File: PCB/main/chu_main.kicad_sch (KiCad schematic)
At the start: 112 parts, among them J1 Conn_01x04, K1 Conn_01x01_Female, K10 Conn_01x01_Female, K11 Conn_01x01_Female, K12 Conn_01x01_Female, K13 Conn_01x01_Female, K14 Conn_01x01_Female, K15 Conn_01x01_Female, K16 Conn_01x01_Female, K17 Conn_01x01_Female, K18 Conn_01x01_Female, K19 Conn_01x01_Female, K2 Conn_01x01_Female, K20 Conn_01x01_Female, K21 Conn_01x01_Female, K22 Conn_01x01_Female, K23 Conn_01x01_Female, K24 Conn_01x01_Female, K25 Conn_01x01_Female, K26 Conn_01x01_Female, K27 Conn_01x01_Female, K28 Conn_01x01_Female, K29 Conn_01x01_Female, K3 Conn_01x01_Female, K30 Conn_01x01_Female, K31 Conn_01x01_Female, K32 Conn_01x01_Female, K4 Conn_01x01_Female, K5 Conn_01x01_Female, K6 Conn_01x01_Female, K7 Conn_01x01_Female, K8 Conn_01x01_Female, K9 Conn_01x01_Female, U0 ChuAcrylic, U1 Pico, U2 PCA9548APW, U3 MPR121QR2_BOARD, U4 MPR121QR2_BOARD, U5 MPR121QR2_BOARD, U8 SN74LV1T34DBV, X1 GP2Y0E03_REAL, X2 GP2Y0E03_REAL, X3 GP2Y0E03_REAL, X4 GP2Y0E03_REAL, X5 GP2Y0E03_REAL

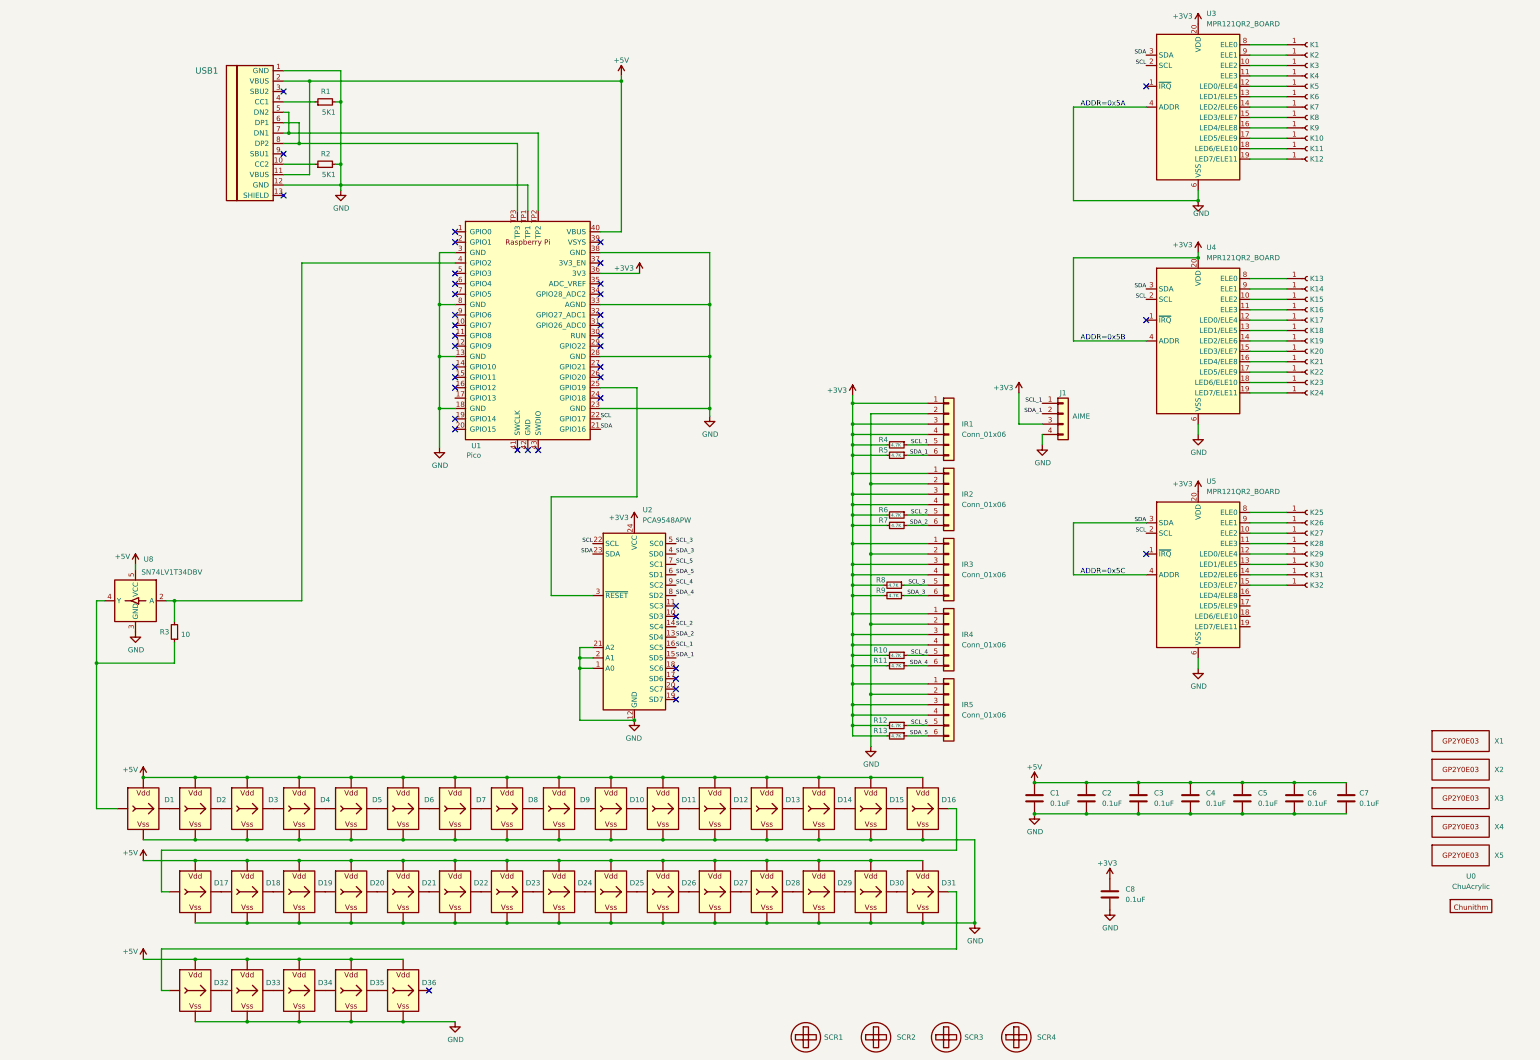
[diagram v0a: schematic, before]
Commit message: wip full size pcb with hc-sr04 ultrasonic sensors
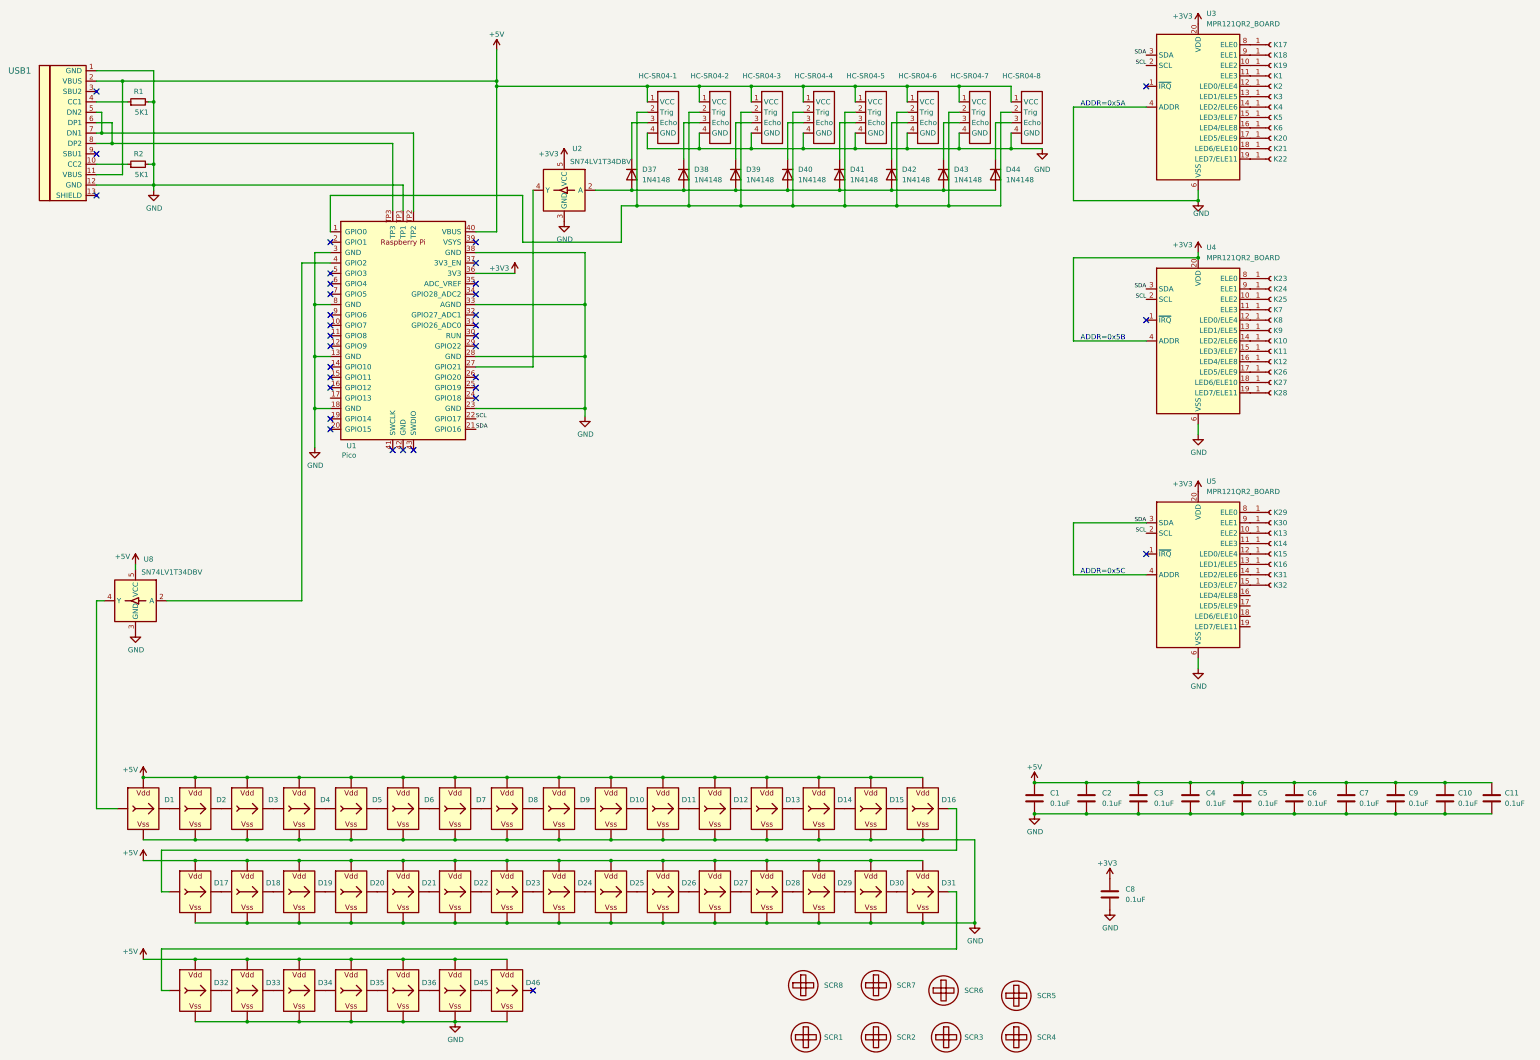
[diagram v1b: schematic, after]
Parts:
- removed IR1, IR2, IR3, IR4, IR5: Conn_01x06, chu_main:GP2Y0E03, symbol Connector_Generic:Conn_01x06
- removed J1: Conn_01x04, chu_main:PN532, symbol Connector_Generic:Conn_01x04
- removed R10, R11, R12, R13, R4, R5, R6, R7, R8, R9: 4.7K, Resistor_SMD:R_0603_1608Metric, symbol Device:R_Small
- removed R3: 10, Resistor_SMD:R_0603_1608Metric, symbol Device:R_Small
- removed U0: ChuAcrylic, chu_main:ChuAcrylic, symbol chu_main:ChuAcrylic
- removed U2: PCA9548APW, Package_SO:TSSOP-24_4.4x7.8mm_P0.65mm, symbol Interface_Expansion:PCA9548APW
- removed X1, X2, X3, X4, X5: GP2Y0E03_REAL, chu_main:GP2Y0E03_REAL, symbol chu_main:GP2Y0E03_REAL
- added C10, C11, C9: 0.1uF, Capacitor_SMD:C_0603_1608Metric_Pad1.08x0.95mm_HandSolder, symbol Device:C
- added D37, D38, D39, D40, D41, D42, D43, D44: 1N4148, Diode_THT:D_DO-35_SOD27_P7.62mm_Horizontal, symbol Diode:1N4148
- added D45, D46: WS2812B_Unified, chu_main:WS2812D-F5, symbol chu_main:WS2812B_Unified
- added HC-SR04-1, HC-SR04-2, HC-SR04-3, HC-SR04-4, HC-SR04-5, HC-SR04-6, HC-SR04-7, HC-SR04-8: ~, HC-SR04:HC-SR04, symbol chu_main:HC-SR04
- added SCR5, SCR6, SCR7, SCR8: ScrewHole, chu_main:MountingHole_3.2mm_M3, symbol iidx_teeny:ScrewHole
- added U2: SN74LV1T34DBV, chu_main:SOT-23-5_Jumper, symbol Logic_LevelTranslator:SN74LV1T34DBV
- D1, D10, D11, D12, D13, D14, D15, D16, D17, D18, D19, D2, D20, D21, D22, D23, D24, D25, D26, D27, D28, D29, D3, D30, D31, D32, D33, D34, D35, D36, D4, D5, D6, D7, D8, D9: footprint chu_main:WS2812B-4020 -> chu_main:WS2812D-F5
- K1, K10, K15, K16, K17, K18, K19, K2, K20, K21, K22, K27, K28, K29, K3, K30, K31, K32, K4, K5, K6, K7, K8, K9: footprint chu_main:ChuKey -> chu_main:Chu_TouchKey
- K11, K14, K23, K26: footprint chu_main:ChuKeyBiasLeft -> chu_main:Chu_TouchKey
- K12, K13, K24, K25: footprint chu_main:ChuKeyBiasRight -> chu_main:Chu_TouchKey
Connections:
- net +3V3: now also U2.5 (VCC)
- net +5V: now also C10.1, C11.1, C9.1, D45.V (VDD), D46.V (VDD), HC-SR04-1.1 (VCC), HC-SR04-2.1 (VCC), HC-SR04-3.1 (VCC), HC-SR04-4.1 (VCC), HC-SR04-5.1 (VCC), HC-SR04-6.1 (VCC), HC-SR04-7.1 (VCC), HC-SR04-8.1 (VCC)
- net GND: now also C10.2, C11.2, C9.2, D45.G (VSS), D46.G (VSS), HC-SR04-1.4 (GND), HC-SR04-2.4 (GND), HC-SR04-3.4 (GND), HC-SR04-4.4 (GND), HC-SR04-5.4 (GND), HC-SR04-6.4 (GND), HC-SR04-7.4 (GND), HC-SR04-8.4 (GND), U2.3 (GND)
- net at U1.1 (GPIO0): now also HC-SR04-1.2 (Trig), HC-SR04-2.2 (Trig), HC-SR04-3.2 (Trig), HC-SR04-4.2 (Trig), HC-SR04-5.2 (Trig), HC-SR04-6.2 (Trig), HC-SR04-7.2 (Trig), HC-SR04-8.2 (Trig)
- net at U1.27 (GPIO21): now also U2.4 (Y)
- net at K11.1 (Pin_1): now also U4.15 (LED3/ELE7); no longer U3.18 (LED6/ELE10)
- net at K3.1 (Pin_1): now also U3.13 (LED1/ELE5); no longer U3.10 (ELE2)
- net at K14.1 (Pin_1): now also U5.11 (ELE3); no longer U4.9 (ELE1)
- net at K29.1 (Pin_1): now also U5.8 (ELE0); no longer U5.12 (LED0/ELE4)
- net at K30.1 (Pin_1): now also U5.9 (ELE1); no longer U5.13 (LED1/ELE5)
- net at K1.1 (Pin_1): now also U3.11 (ELE3); no longer U3.8 (ELE0)
- net at K7.1 (Pin_1): now also U4.11 (ELE3); no longer U3.14 (LED2/ELE6)
- net at K27.1 (Pin_1): now also U4.18 (LED6/ELE10); no longer U5.10 (ELE2)
- net at K19.1 (Pin_1): now also U3.10 (ELE2); no longer U4.14 (LED2/ELE6)
- net at K6.1 (Pin_1): now also U3.16 (LED4/ELE8); no longer U3.13 (LED1/ELE5)
- net at K15.1 (Pin_1): now also U5.12 (LED0/ELE4); no longer U4.10 (ELE2)
- net at K5.1 (Pin_1): now also U3.15 (LED3/ELE7); no longer U3.12 (LED0/ELE4)
- net at K23.1 (Pin_1): now also U4.8 (ELE0); no longer U4.18 (LED6/ELE10)
- net at K16.1 (Pin_1): now also U5.13 (LED1/ELE5); no longer U4.11 (ELE3)
- net at U4.12 (LED0/ELE4): now also K8.1 (Pin_1); no longer K17.1 (Pin_1)
- net at U4.13 (LED1/ELE5): now also K9.1 (Pin_1); no longer K18.1 (Pin_1)
- net at K20.1 (Pin_1): now also U3.17 (LED5/ELE9); no longer U4.15 (LED3/ELE7)
- net at U4.16 (LED4/ELE8): now also K12.1 (Pin_1); no longer K21.1 (Pin_1)
- net at U4.17 (LED5/ELE9): now also K26.1 (Pin_1); no longer K22.1 (Pin_1)
- net at U4.19 (LED7/ELE11): now also K28.1 (Pin_1); no longer K24.1 (Pin_1)
- net at K13.1 (Pin_1): now also U5.10 (ELE2); no longer U4.8 (ELE0)
- net at K10.1 (Pin_1): now also U4.14 (LED2/ELE6); no longer U3.17 (LED5/ELE9)
- net at K4.1 (Pin_1): now also U3.14 (LED2/ELE6); no longer U3.11 (ELE3)
- net at U3.19 (LED7/ELE11): now also K22.1 (Pin_1); no longer K12.1 (Pin_1)
- net at K2.1 (Pin_1): now also U3.12 (LED0/ELE4); no longer U3.9 (ELE1)
- net at K25.1 (Pin_1): now also U4.10 (ELE2); no longer U5.8 (ELE0)
- net at D36.O (Out): now also D45.I (In)
- new net: D44.1 (K), HC-SR04-8.3 (Echo)
- new net: D37.1 (K), HC-SR04-1.3 (Echo)
- new net: D43.1 (K), HC-SR04-7.3 (Echo)
- new net: D37.2 (A), D38.2 (A), D39.2 (A), D40.2 (A), D41.2 (A), D42.2 (A), D43.2 (A), D44.2 (A), U2.2 (A)
- new net: D45.O (Out), D46.I (In)
- new net: D42.1 (K), HC-SR04-6.3 (Echo)
- new net: D41.1 (K), HC-SR04-5.3 (Echo)
- new net: D40.1 (K), HC-SR04-4.3 (Echo)
- new net: K24.1 (Pin_1), U4.9 (ELE1)
- new net: K17.1 (Pin_1), U3.8 (ELE0)
- new net: K21.1 (Pin_1), U3.18 (LED6/ELE10)
- new net: K18.1 (Pin_1), U3.9 (ELE1)
- new net: D39.1 (K), HC-SR04-3.3 (Echo)
- new net: D38.1 (K), HC-SR04-2.3 (Echo)
- no-connect marks 41 -> 34
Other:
- moved on the sheet: K1, K10, K11, K12, K13, K14, K15, K16, K17, K18, K19, K2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
